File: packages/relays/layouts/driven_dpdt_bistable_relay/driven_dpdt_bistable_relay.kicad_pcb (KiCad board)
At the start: 2 copper layers, 9 parts

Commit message: [Publish] Rebuild modules (with no dep on upstream atopile pr) (#5)
* Fixes image link on published packages
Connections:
- C5 pad 1: hv-1 -> hv
- C5 pad 2: gnd -> gnd-1
- C6 pad 1: hv-1 -> hv
- C6 pad 2: gnd -> gnd-1
- C8 pad 1: hv -> hv-1
- C8 pad 2: gnd-1 -> gnd
- D1 pad 2: line -> line-1
- D2 pad 2: line-4 -> line-6
- R1 pad 2: gnd -> gnd-1
- R3 pad 2: gnd -> gnd-1
- RELAY1 pad 1: gnd-1 -> gnd
- RELAY1 pad 2: line-3 -> line-7
- RELAY1 pad 3: line-1 -> line-4
- RELAY1 pad 4: line-7 -> line-3
- RELAY1 pad 6: line-6 -> line
- RELAY1 pad 8: hv -> hv-1
- U7 pad 2: line -> line-1
- U7 pad 3: line-4 -> line-6
- U7 pad 4: hv-1 -> hv
- U7 pad 5: gnd-1 -> gnd
- U7 pad 6: gnd -> gnd-1
- U7 pad 7: gnd -> gnd-1
- U7 pad 8: hv -> hv-1
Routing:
- net gnd-1: track 6.34 -> 0.00 mm
- net gnd: track 0.00 -> 6.34 mm
- net line-6: track 0.00 -> 4.81 mm
- net line-4: track 4.81 -> 0.00 mm
- net line-1: track 0.00 -> 4.81 mm
- net line: track 4.81 -> 0.00 mm
- net hv-1: track 2.61 -> 6.34 mm
- net hv: track 6.34 -> 2.61 mm
- added copper zone on F.Cu, net gnd-1
- removed copper zone on F.Cu, net gnd
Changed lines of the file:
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@@
     (net 1 "line-5")
     (net 2 "net")
-    (net 3 "gnd-1")
-    (net 4 "line-6")
-    (net 5 "line-1")
+    (net 3 "gnd")
+    (net 4 "line")
+    (net 5 "line-4")
     (net 6 "line-2")
-    (net 7 "hv")
-    (net 8 "line-3")
-    (net 9 "line-7")
+    (net 7 "hv-1")
+    (net 8 "line-7")
+    (net 9 "line-3")
     (net 10 "led_indicator_b.led-cathode")
     (net 11 "led_indicator_a.led-cathode")
-    (net 12 "line-4")
-    (net 13 "line")
-    (net 14 "hv-1")
-    (net 15 "gnd")
+    (net 12 "line-6")
+    (net 13 "line-1")
+    (net 14 "hv")
+    (net 15 "gnd-1")
     (footprint "atopile:LED0603-RD-c81ffb"
         (layer "F.Cu")
@@
             (size 0.8 0.8)
             (layers "F.Cu" "F.Mask" "F.Paste")
-            (net 13 "line")
+            (net 13 "line-1")
         )
         (embedded_fonts no)
@@
             (size 0.57 0.54)
             (layers "F.Cu" "F.Mask" "F.Paste")
-            (net 15 "gnd")
+            (net 15 "gnd-1")
         )
         (embedded_fonts no)
@@
             (size 0.79 0.54)
             (layers "F.Cu" "F.Mask" "F.Paste")
-            (net 7 "hv")
+            (net 7 "hv-1")
         )
         (pad "2" smd rect
@@
             (size 0.79 0.54)
             (layers "F.Cu" "F.Mask" "F.Paste")
-            (net 3 "gnd-1")
+            (net 3 "gnd")
         )
         (embedded_fonts no)
@@
             (size 0.79 0.54)
             (layers "F.Cu" "F.Mask" "F.Paste")
-            (net 14 "hv-1")
+            (net 14 "hv")
         )
         (pad "2" smd rect
@@
             (size 0.79 0.54)
             (layers "F.Cu" "F.Mask" "F.Paste")
-            (net 15 "gnd")
+            (net 15 "gnd-1")
         )
         (embedded_fonts no)
@@
             (size 0.63 1.86)
             (layers "F.Cu" "F.Mask" "F.Paste")
-            (net 13 "line")
+            (net 13 "line-1")
         )
         (pad "3" smd oval
@@
             (size 0.63 1.86)
             (layers "F.Cu" "F.Mask" "F.Paste")
-            (net 12 "line-4")
+            (net 12 "line-6")
         )
         (pad "4" smd oval
@@
             (size 0.63 1.86)
             (layers "F.Cu" "F.Mask" "F.Paste")
-            (net 14 "hv-1")
+            (net 14 "hv")
         )
         (pad "5" smd oval
@@
             (size 0.63 1.86)
             (layers "F.Cu" "F.Mask" "F.Paste")
-            (net 3 "gnd-1")
+            (net 3 "gnd")
         )
         (pad "6" smd oval
@@
             (size 0.63 1.86)
             (layers "F.Cu" "F.Mask" "F.Paste")
-            (net 15 "gnd")
+            (net 15 "gnd-1")
         )
         (pad "7" smd oval
@@
             (size 0.63 1.86)
             (layers "F.Cu" "F.Mask" "F.Paste")
-            (net 15 "gnd")
+            (net 15 "gnd-1")
         )
         (pad "8" smd oval
@@
             (size 0.63 1.86)
             (layers "F.Cu" "F.Mask" "F.Paste")
-            (net 7 "hv")
+            (net 7 "hv-1")
         )
         (embedded_fonts no)
@@
             (size 0.57 0.54)
             (layers "F.Cu" "F.Mask" "F.Paste")
-            (net 15 "gnd")
+            (net 15 "gnd-1")
         )
         (embedded_fonts no)
@@
             (size 0.8 0.8)
             (layers "F.Cu" "F.Mask" "F.Paste")
-            (net 12 "line-4")
+            (net 12 "line-6")
         )
         (embedded_fonts no)
@@
             (size 0.79 0.54)
             (layers "F.Cu" "F.Mask" "F.Paste")
-            (net 14 "hv-1")
+            (net 14 "hv")
         )
         (pad "2" smd rect
@@
             (size 0.79 0.54)
             (layers "F.Cu" "F.Mask" "F.Paste")
-            (net 15 "gnd")
+            (net 15 "gnd-1")
         )
         (embedded_fonts no)
@@
             (size 0.8 1.8)
             (layers "F.Cu" "F.Mask" "F.Paste")
-            (net 3 "gnd-1")
+            (net 3 "gnd")
         )
         (pad "2" smd rect
@@
             (size 0.8 1.8)
             (layers "F.Cu" "F.Mask" "F.Paste")
-            (net 8 "line-3")
+            (net 8 "line-7")
         )
         (pad "3" smd rect
@@
             (size 0.8 1.8)
             (layers "F.Cu" "F.Mask" "F.Paste")
-            (net 5 "line-1")
+            (net 5 "line-4")
         )
         (pad "4" smd rect
@@
             (size 0.8 1.8)
             (layers "F.Cu" "F.Mask" "F.Paste")
-            (net 9 "line-7")
+            (net 9 "line-3")
         )
         (pad "5" smd rect
@@
             (size 0.8 1.8)
             (layers "F.Cu" "F.Mask" "F.Paste")
-            (net 4 "line-6")
+            (net 4 "line")
         )
         (pad "7" smd rect
@@
             (size 0.8 1.8)
             (layers "F.Cu" "F.Mask" "F.Paste")
-            (net 7 "hv")
+            (net 7 "hv-1")
         )
         (embedded_fonts no)
@@
     (zone
         (net 15)
-        (net_name "gnd")
+        (net_name "gnd-1")
         (layers "F.Cu")
         (hatch edge 0.5)

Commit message: Add DrivenDPDTBistableRelayScrewTerminal
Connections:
- RELAY1 pad 5: line-2 -> line-1
- RELAY1 pad 7: line-5 -> line-6
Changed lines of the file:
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@@
     )
     (net 0 "")
-    (net 1 "line-5")
+    (net 1 "line-6")
     (net 2 "net")
     (net 3 "gnd")
@@
             (size 0.8 1.8)
             (layers "F.Cu" "F.Mask" "F.Paste")
-            (net 6 "line-2")
+            (net 6 "line-1")
         )
         (pad "6" smd rect
@@
             (size 0.8 1.8)
             (layers "F.Cu" "F.Mask" "F.Paste")
-            (net 1 "line-5")
+            (net 1 "line-6")
         )
         (pad "8" smd rect

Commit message: Rebuild relays package
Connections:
- D1 pad 2: line-1 -> line
- D2 pad 2: line-6 -> line-4
- RELAY1 pad 2: line-7 -> line-2
- RELAY1 pad 3: line-4 -> line-3
- RELAY1 pad 4: line-3 -> line-1
- RELAY1 pad 5: line-1 -> line-7
- RELAY1 pad 6: line -> line-6
- RELAY1 pad 7: line-6 -> line-5
- U7 pad 2: line-1 -> line
- U7 pad 3: line-6 -> line-4
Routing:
- net line-6: track 4.81 -> 0.00 mm
- net line-4: track 0.00 -> 4.81 mm
- net line-1: track 4.81 -> 0.00 mm
- net line: track 0.00 -> 4.81 mm
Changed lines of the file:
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@@
     )
     (net 0 "")
-    (net 1 "line-6")
     (net 2 "net")
     (net 3 "gnd")
-    (net 4 "line")
-    (net 5 "line-4")
-    (net 6 "line-2")
+    (net 4 "line-6")
+    (net 5 "line-3")
     (net 7 "hv-1")
-    (net 8 "line-7")
-    (net 9 "line-3")
+    (net 8 "line-2")
+    (net 9 "line-1")
     (net 10 "led_indicator_b.led-cathode")
     (net 11 "led_indicator_a.led-cathode")
-    (net 12 "line-6")
-    (net 13 "line-1")
+    (net 12 "line-4")
+    (net 13 "line")
     (net 14 "hv")
     (net 15 "gnd-1")
+    (net 16 "line-7")
+    (net 17 "line-5")
     (footprint "atopile:LED0603-RD-c81ffb"
         (layer "F.Cu")
@@
             (size 0.8 0.8)
             (layers "F.Cu" "F.Mask" "F.Paste")
-            (net 13 "line-1")
+            (net 13 "line")
         )
         (embedded_fonts no)
@@
             (size 0.63 1.86)
             (layers "F.Cu" "F.Mask" "F.Paste")
-            (net 13 "line-1")
+            (net 13 "line")
         )
         (pad "3" smd oval
@@
             (size 0.63 1.86)
             (layers "F.Cu" "F.Mask" "F.Paste")
-            (net 12 "line-6")
+            (net 12 "line-4")
         )
         (pad "4" smd oval
@@
             (size 0.8 0.8)
             (layers "F.Cu" "F.Mask" "F.Paste")
-            (net 12 "line-6")
+            (net 12 "line-4")
         )
         (embedded_fonts no)
@@
             (size 0.8 1.8)
             (layers "F.Cu" "F.Mask" "F.Paste")
-            (net 8 "line-7")
+            (net 8 "line-2")
         )
         (pad "3" smd rect
@@
             (size 0.8 1.8)
             (layers "F.Cu" "F.Mask" "F.Paste")
-            (net 5 "line-4")
+            (net 5 "line-3")
         )
         (pad "4" smd rect
@@
             (size 0.8 1.8)
             (layers "F.Cu" "F.Mask" "F.Paste")
-            (net 9 "line-3")
+            (net 9 "line-1")
         )
         (pad "5" smd rect
@@
             (size 0.8 1.8)
             (layers "F.Cu" "F.Mask" "F.Paste")
-            (net 6 "line-1")
+            (net 16 "line-7")
         )
         (pad "6" smd rect
@@
             (size 0.8 1.8)
             (layers "F.Cu" "F.Mask" "F.Paste")
-            (net 4 "line")
+            (net 4 "line-6")
         )
         (pad "7" smd rect
@@
             (size 0.8 1.8)
             (layers "F.Cu" "F.Mask" "F.Paste")
-            (net 1 "line-6")
+            (net 17 "line-5")
         )
         (pad "8" smd rect

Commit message: Rebuild all
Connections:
- C5 pad 2: gnd-1 -> gnd
- C6 pad 2: gnd-1 -> gnd
- C8 pad 2: gnd -> gnd-1
- D1 pad 2: line -> line-7
- D2 pad 2: line-4 -> line-2
- R1 pad 2: gnd-1 -> gnd
- R3 pad 2: gnd-1 -> gnd
- RELAY1 pad 1: gnd -> gnd-1
- RELAY1 pad 2: line-2 -> line-5
- RELAY1 pad 3: line-3 -> line-6
- RELAY1 pad 4: line-1 -> line-4
- RELAY1 pad 5: line-7 -> line-3
- RELAY1 pad 6: line-6 -> line
- RELAY1 pad 7: line-5 -> line-1
- U7 pad 2: line -> line-7
- U7 pad 3: line-4 -> line-2
- U7 pad 5: gnd -> gnd-1
- U7 pad 6: gnd-1 -> gnd
- U7 pad 7: gnd-1 -> gnd
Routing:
- net gnd-1: track 0.00 -> 6.34 mm
- net gnd: track 6.34 -> 0.00 mm
- net line-7: track 0.00 -> 4.81 mm
- net line-4: track 4.81 -> 0.00 mm
- net line-2: track 0.00 -> 4.81 mm
- net line: track 4.81 -> 0.00 mm
- added copper zone on F.Cu, net gnd
- removed copper zone on F.Cu, net gnd-1
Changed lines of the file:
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@@
     (net 0 "")
     (net 2 "net")
-    (net 3 "gnd")
-    (net 4 "line-6")
-    (net 5 "line-3")
+    (net 3 "gnd-1")
+    (net 4 "line")
+    (net 5 "line-6")
     (net 7 "hv-1")
-    (net 8 "line-2")
-    (net 9 "line-1")
+    (net 8 "line-5")
+    (net 9 "line-4")
     (net 10 "led_indicator_b.led-cathode")
     (net 11 "led_indicator_a.led-cathode")
-    (net 12 "line-4")
-    (net 13 "line")
+    (net 12 "line-2")
+    (net 13 "line-7")
     (net 14 "hv")
-    (net 15 "gnd-1")
-    (net 16 "line-7")
-    (net 17 "line-5")
+    (net 15 "gnd")
+    (net 16 "line-3")
+    (net 17 "line-1")
     (footprint "atopile:LED0603-RD-c81ffb"
         (layer "F.Cu")
@@
             (size 0.8 0.8)
             (layers "F.Cu" "F.Mask" "F.Paste")
-            (net 13 "line")
+            (net 13 "line-7")
         )
         (embedded_fonts no)
@@
             (size 0.57 0.54)
             (layers "F.Cu" "F.Mask" "F.Paste")
-            (net 15 "gnd-1")
+            (net 15 "gnd")
         )
         (embedded_fonts no)
@@
             (size 0.79 0.54)
             (layers "F.Cu" "F.Mask" "F.Paste")
-            (net 3 "gnd")
+            (net 3 "gnd-1")
         )
         (embedded_fonts no)
@@
             (size 0.79 0.54)
             (layers "F.Cu" "F.Mask" "F.Paste")
-            (net 15 "gnd-1")
+            (net 15 "gnd")
         )
         (embedded_fonts no)
@@
             (size 0.63 1.86)
             (layers "F.Cu" "F.Mask" "F.Paste")
-            (net 13 "line")
+            (net 13 "line-7")
         )
         (pad "3" smd oval
@@
             (size 0.63 1.86)
             (layers "F.Cu" "F.Mask" "F.Paste")
-            (net 12 "line-4")
+            (net 12 "line-2")
         )
         (pad "4" smd oval
@@
             (size 0.63 1.86)
             (layers "F.Cu" "F.Mask" "F.Paste")
-            (net 3 "gnd")
+            (net 3 "gnd-1")
         )
         (pad "6" smd oval
@@
             (size 0.63 1.86)
             (layers "F.Cu" "F.Mask" "F.Paste")
-            (net 15 "gnd-1")
+            (net 15 "gnd")
         )
         (pad "7" smd oval
@@
             (size 0.63 1.86)
             (layers "F.Cu" "F.Mask" "F.Paste")
-            (net 15 "gnd-1")
+            (net 15 "gnd")
         )
         (pad "8" smd oval
@@
             (size 0.57 0.54)
             (layers "F.Cu" "F.Mask" "F.Paste")
-            (net 15 "gnd-1")
+            (net 15 "gnd")
         )
         (embedded_fonts no)
@@
             (size 0.8 0.8)
             (layers "F.Cu" "F.Mask" "F.Paste")
-            (net 12 "line-4")
+            (net 12 "line-2")
         )
         (embedded_fonts no)
@@
             (size 0.79 0.54)
             (layers "F.Cu" "F.Mask" "F.Paste")
-            (net 15 "gnd-1")
+            (net 15 "gnd")
         )
         (embedded_fonts no)
@@
             (size 0.8 1.8)
             (layers "F.Cu" "F.Mask" "F.Paste")
-            (net 3 "gnd")
+            (net 3 "gnd-1")
         )
         (pad "2" smd rect
@@
             (size 0.8 1.8)
             (layers "F.Cu" "F.Mask" "F.Paste")
-            (net 8 "line-2")
+            (net 8 "line-5")
         )
         (pad "3" smd rect
@@
             (size 0.8 1.8)
             (layers "F.Cu" "F.Mask" "F.Paste")
-            (net 5 "line-3")
+            (net 5 "line-6")
         )
         (pad "4" smd rect
@@
             (size 0.8 1.8)
             (layers "F.Cu" "F.Mask" "F.Paste")
-            (net 9 "line-1")
+            (net 9 "line-4")
         )
         (pad "5" smd rect
@@
             (size 0.8 1.8)
             (layers "F.Cu" "F.Mask" "F.Paste")
-            (net 16 "line-7")
+            (net 16 "line-3")
         )
         (pad "6" smd rect
@@
             (size 0.8 1.8)
             (layers "F.Cu" "F.Mask" "F.Paste")
-            (net 4 "line-6")
+            (net 4 "line")
         )
         (pad "7" smd rect
@@
             (size 0.8 1.8)
             (layers "F.Cu" "F.Mask" "F.Paste")
-            (net 17 "line-5")
+            (net 17 "line-1")
         )
         (pad "8" smd rect
@@
     (zone
         (net 15)
-        (net_name "gnd-1")
+        (net_name "gnd")
         (layers "F.Cu")
         (hatch edge 0.5)

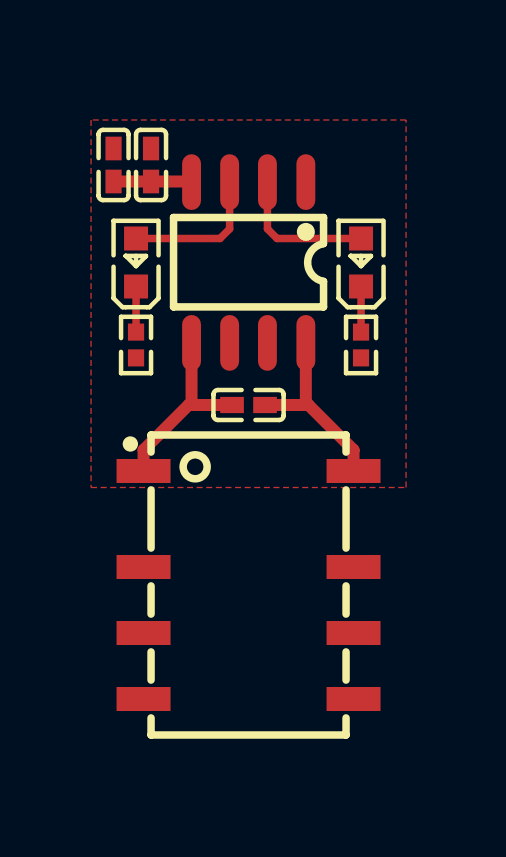
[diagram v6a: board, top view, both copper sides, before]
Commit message: Fix wrong logic reference. Split driver into own module
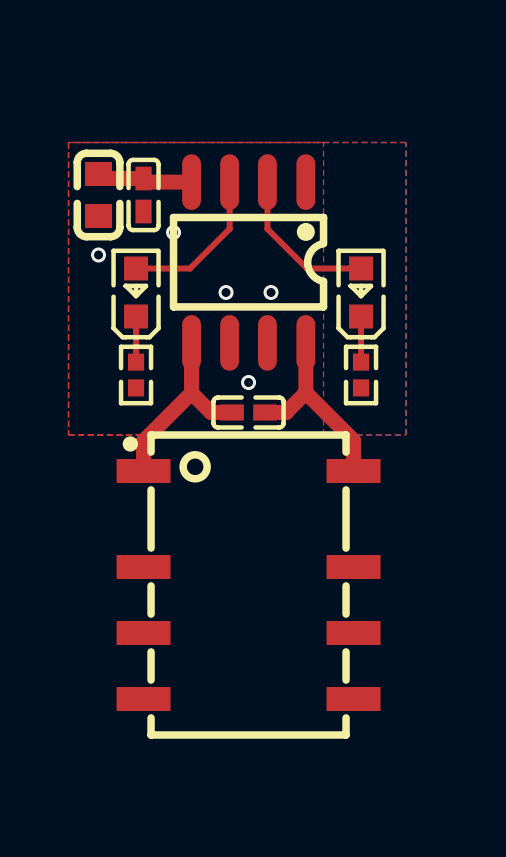
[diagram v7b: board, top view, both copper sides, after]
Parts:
- removed C5, C6, C8: 100nF ±10% 16V X7R, atopile:C0402-b3ef17
- removed U7: , atopile:SOP-8_L4.9-W3.9-P1.27-LS6.0-BL-0d1ac6
- added C1: 100nF ±10% 16V X7R, atopile:C0402-b3ef17, F.Cu at (-3.50, -13.0)
- added C2: 4.7µF ±10% 16V X5R, atopile:C0603-bd72f6, F.Cu at (-5.00, -13.0)
- added C3: 100pF ±5% 50V C0G, atopile:C0402-b3ef17, F.Cu at (0.00, -5.75)
- added U1: , atopile:SOP-8_L4.9-W3.9-P1.27-LS6.0-BL-0d1ac6, F.Cu at (0.00, -10.8)
- moved D1 1.00 mm to (3.75, -9.75)
- moved D2 1.00 mm to (-3.75, -9.75)
- moved R1 1.00 mm to (3.75, -7.00)
- moved R3 1.00 mm to (-3.75, -7.00)
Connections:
- D1 pad 2: line-7 -> line-6
- RELAY1 pad 2: line-5 -> line
- RELAY1 pad 3: line-6 -> line-4
- RELAY1 pad 4: line-4 -> line-5
- RELAY1 pad 5: line-3 -> line-7
- RELAY1 pad 6: line -> line-3
- RELAY1 pad 8: hv-1 -> OUTA
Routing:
- net OUTA: track 0.00 -> 6.56 mm
- net hv-1: track 6.34 -> 0.00 mm
- net line-6: track 0.00 -> 5.23 mm
- net line-7: track 4.81 -> 0.00 mm
- net hv: track 2.61 -> 3.21 mm
- net gnd: vias 0 -> 5
- added copper zone on B.Cu, net gnd

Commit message: Manually fix fp lib tables
fix some small bugs
fix package only modules (e.g. logos)
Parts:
- removed D1, D2: , atopile:LED0603-RD-c81ffb
- removed R3: 1kΩ ±1% 62.5mW, atopile:R0402-56259e
- added R2: 10kΩ ±1% 62.5mW, UNI_ROYAL_0402WGF1002TCE:R0402, F.Cu at (-3.75, -7.00)
- added U2: 2V, Hubei_KENTO_Elec_KT_0603R:LED0603-RD, F.Cu at (3.75, -9.75)
- added U3: 2.75V, Hubei_KENTO_Elec_KT_0603G:LED0603-RD, F.Cu at (-3.75, -9.75)
- C1: footprint atopile:C0402-b3ef17 -> Samsung_Electro_Mechanics_CL05B104KO5NNNC:C0402
- C2: footprint atopile:C0603-bd72f6 -> Samsung_Electro_Mechanics_CL10A475KO8NNNC:C0603
- C3: footprint atopile:C0402-b3ef17 -> FH_0402CG101J500NT:C0402
- R1: value 1kΩ ±1% 62.5mW -> 10kΩ ±1% 62.5mW; footprint atopile:R0402-56259e -> UNI_ROYAL_0402WGF1002TCE:R0402
- RELAY1: footprint atopile:RELAY-SMD_G6KU-2F-Y-bd7654 -> Omron_Electronics_G6KU_2F_Y_TR_DC5:RELAY-SMD_G6KU-2F-Y
- U1: footprint atopile:SOP-8_L4.9-W3.9-P1.27-LS6.0-BL-0d1ac6 -> Shenzhen_Fuman_Elec_TC118S:SOP-8_L4.9-W3.9-P1.27-LS6.0-BL
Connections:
- C1 pad 2: gnd -> gnd-1
- C2 pad 2: gnd -> gnd-1
- C3 pad 2: gnd-1 -> gnd
- R1 pad 1: led_indicator_a.led-cathode -> cathode-1
- R1 pad 2: gnd -> gnd-1
- RELAY1 pad 1: gnd-1 -> gnd
- RELAY1 pad 2: line -> line-1
- RELAY1 pad 4: line-5 -> line-2
- RELAY1 pad 5: line-7 -> line-5
- RELAY1 pad 7: line-1 -> line
- U1 pad 2: line-6 -> anode
- U1 pad 3: line-2 -> anode-1
- U1 pad 5: gnd-1 -> gnd
- U1 pad 6: gnd -> gnd-1
- U1 pad 7: gnd -> gnd-1
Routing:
- net gnd-1: track 6.55 -> 0.00 mm
- net gnd: track 0.00 -> 6.55 mm, vias 5 -> 0
- net line-6: track 5.23 -> 0.00 mm
- net anode: track 0.00 -> 5.23 mm
- net line-2: track 5.23 -> 0.00 mm
- net anode-1: track 0.00 -> 5.23 mm
- net led_indicator_b.led-cathode: track 1.52 -> 0.00 mm
- net led_indicator_a.led-cathode: track 1.52 -> 0.00 mm
- net cathode-1: track 0.00 -> 1.52 mm
- net cathode: track 0.00 -> 1.52 mm
- net (no net): vias 0 -> 5
- added copper zone on F.Cu, net (none)
- added copper zone on B.Cu, net gnd-1
- added copper zone on F.Cu, net gnd-1
- removed copper zone on B.Cu, net gnd
- removed copper zone on F.Cu, net gnd
